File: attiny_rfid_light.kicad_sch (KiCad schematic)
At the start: 26 parts, among them IC1 EM4095, U1 ESP32-WROOM-32, U2 NCP1117-3.3_SOT223

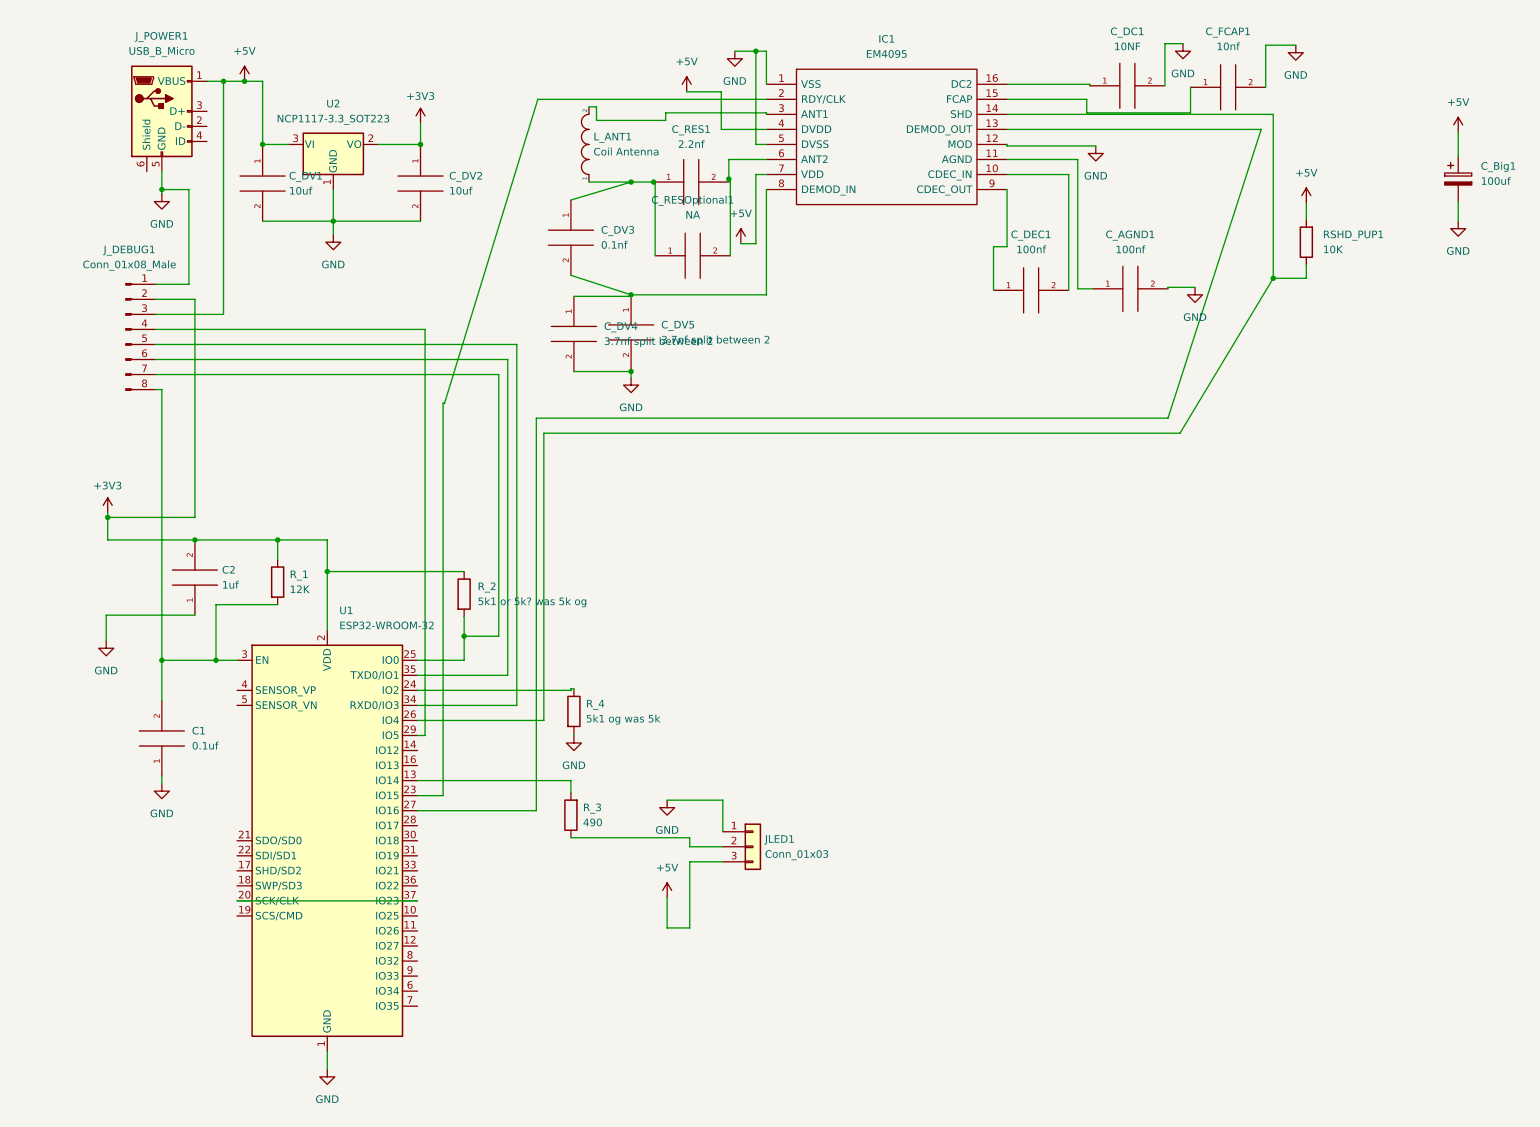
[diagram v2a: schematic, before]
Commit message: updated values to match place values
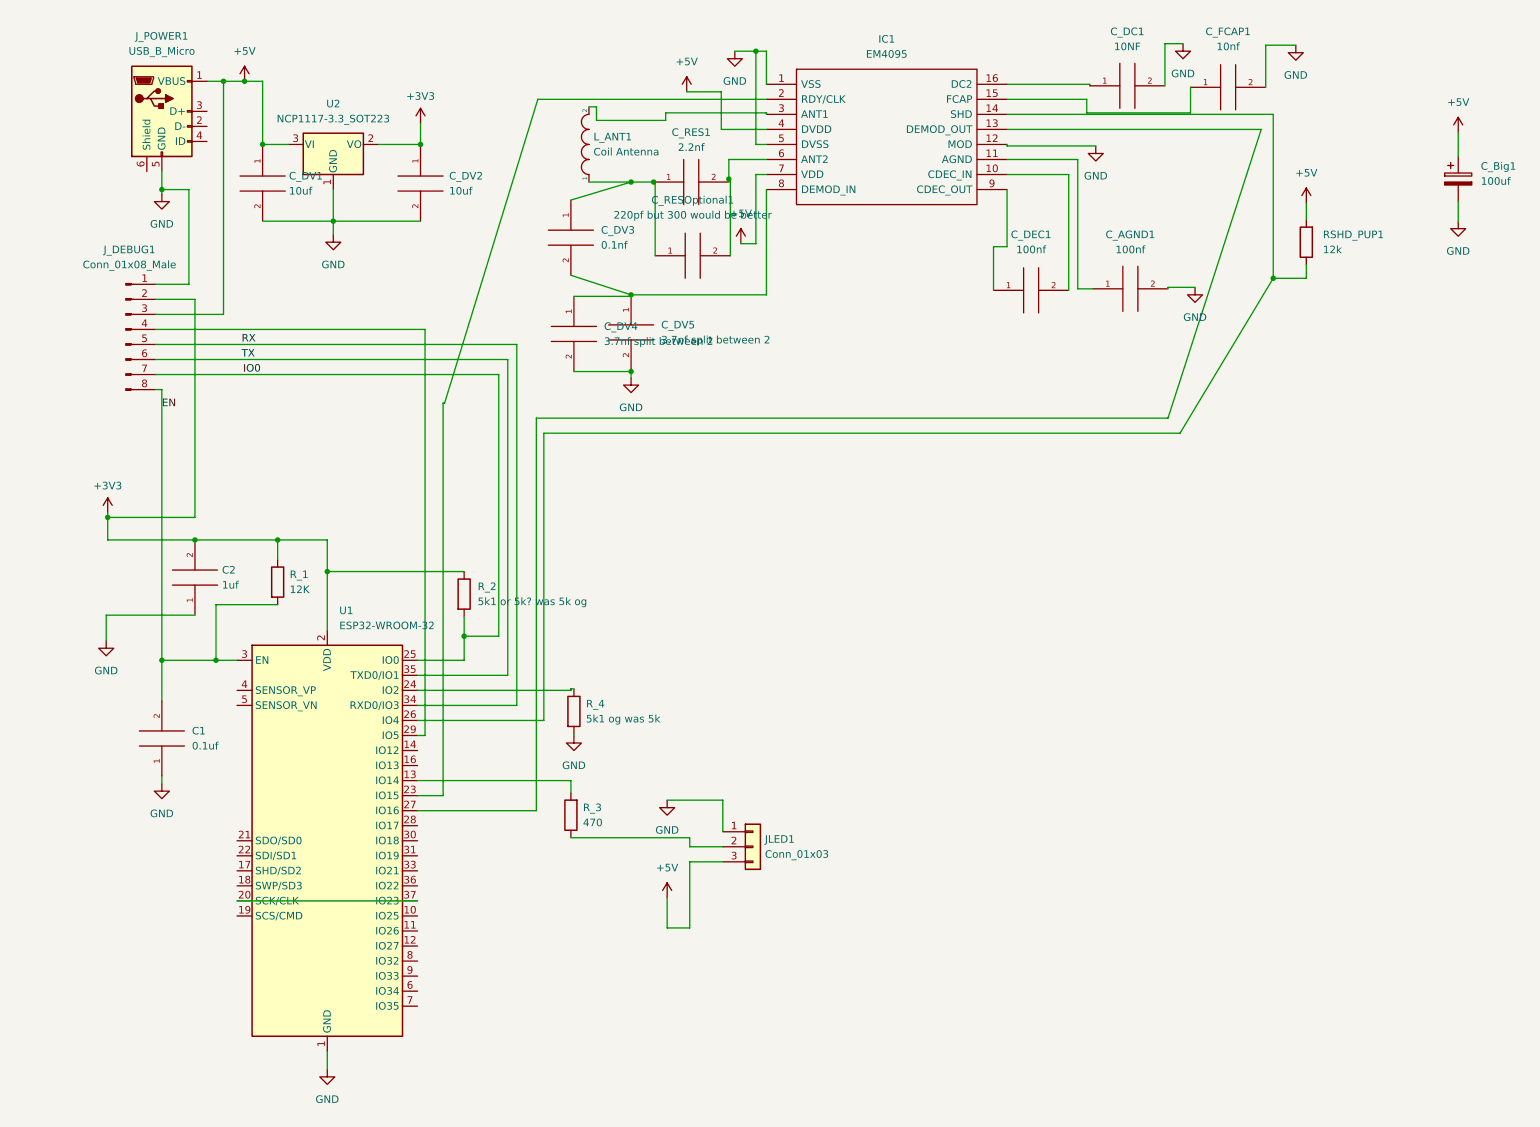
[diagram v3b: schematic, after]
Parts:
- C_RESOptional1: value NA -> 220pf but 300 would be better
- RSHD_PUP1: value 10K -> 12k
- R_3: value 490 -> 470
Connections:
- net RX: now reaches J_DEBUG1.5 (Pin_5), U1.34 (RXD0/IO3)
- net TX: now reaches J_DEBUG1.6 (Pin_6), U1.35 (TXD0/IO1)
- net IO0: now reaches J_DEBUG1.7 (Pin_7), R_2.2, U1.25 (IO0)
- net EN: now reaches C1.2, J_DEBUG1.8 (Pin_8), R_1.2, U1.3 (EN)
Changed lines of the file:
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@@
     (stroke (width 0) (type default) (color 0 0 0 0))
+  )
+  (label "TX" (at 43.942 70.104 0)
+    (effects (font (size 1.27 1.27)) (justify left bottom))
+  )
+  (label "IO0" (at 44.196 72.644 0)
+    (effects (font (size 1.27 1.27)) (justify left bottom))
+  )
+  (label "RX" (at 43.942 67.564 0)
+    (effects (font (size 1.27 1.27)) (justify left bottom))
+  )
+  (label "EN" (at 30.48 78.486 0)
+    (effects (font (size 1.27 1.27)) (justify left bottom))
   )
   (symbol (lib_id "Connector:Conn_01x08_Male") (at 24.384 65.024 0) (unit 1)
@@
       (effects (font (size 1.27 1.27)) (justify right))
     )
-    (property "Value" "10K" (id 1) (at 226.568 51.5619 0)
+    (property "Value" "12k" (id 1) (at 226.568 51.5619 0)
       (effects (font (size 1.27 1.27)) (justify right))
     )
@@
     (in_bom yes) (on_board yes) (fields_autoplaced)
     (property "Reference" "C_RESOptional1" (id 0) (at 120.142 43.18 90))
-    (property "Value" "NA" (id 1) (at 120.142 45.72 90))
+    (property "Value" "220pf but 300 would be better" (id 1) (at 120.142 45.72 90))
     (property "Footprint" "Capacitor_SMD:C_0805_2012Metric_Pad1.18x1.45mm_HandSolder" (id 2) (at 120.142 52.578 0)
       (effects (font (size 1.27 1.27)) hide)
@@
       (effects (font (size 1.27 1.27)) (justify right))
     )
-    (property "Value" "490" (id 1) (at 101.6 148.3359 0)
+    (property "Value" "470" (id 1) (at 101.6 148.3359 0)
       (effects (font (size 1.27 1.27)) (justify right))
     )
@@
   (symbol (lib_id "pspice:C") (at 119.888 40.132 90) (unit 1)
     (in_bom yes) (on_board yes) (fields_autoplaced)
-    (property "Reference" "C_RES1" (id 0) (at 119.888 31.242 90))
-    (property "Value" "2.2nf" (id 1) (at 119.888 33.782 90))
+    (property "Reference" "C_RES1" (id 0) (at 119.888 31.75 90))
+    (property "Value" "2.2nf" (id 1) (at 119.888 34.29 90))
     (property "Footprint" "Capacitor_SMD:C_0805_2012Metric_Pad1.18x1.45mm_HandSolder" (id 2) (at 119.888 40.132 0)
       (effects (font (size 1.27 1.27)) hide)
@@
     )
     (path "/9f822722-8d50-42f5-a09c-1e6f990511b7"
-      (reference "C_RESOptional1") (unit 1) (value "NA") (footprint "Capacitor_SMD:C_0805_2012Metric_Pad1.18x1.45mm_HandSolder")
+      (reference "C_RESOptional1") (unit 1) (value "220pf but 300 would be better") (footprint "Capacitor_SMD:C_0805_2012Metric_Pad1.18x1.45mm_HandSolder")
     )
     (path "/72ff0485-f700-4243-a66c-13414af86c8f"
@@
     )
     (path "/81c65984-9f9d-492c-82f9-bbe24b88ebc2"
-      (reference "RSHD_PUP1") (unit 1) (value "10K") (footprint "Resistor_SMD:R_0805_2012Metric_Pad1.20x1.40mm_HandSolder")
+      (reference "RSHD_PUP1") (unit 1) (value "12k") (footprint "Resistor_SMD:R_0805_2012Metric_Pad1.20x1.40mm_HandSolder")
     )
     (path "/b2b8605e-6475-43cb-8fde-09cbdf493df9"
@@
     )
     (path "/ae4d83e7-2b1c-4a1b-a2e3-a202e2758c5c"
-      (reference "R_3") (unit 1) (value "490") (footprint "Resistor_SMD:R_0805_2012Metric_Pad1.20x1.40mm_HandSolder")
+      (reference "R_3") (unit 1) (value "470") (footprint "Resistor_SMD:R_0805_2012Metric_Pad1.20x1.40mm_HandSolder")
     )
     (path "/6eacda91-754b-4c18-b3d0-a8600716fb2d"

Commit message: v4
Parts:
- removed J_DEBUG1: Conn_01x08_Male, Connector_PinHeader_2.54mm:PinHeader_1x08_P2.54mm_Vertical, symbol Connector:Conn_01x08_Male
- added C_RESC1: optional, Capacitor_SMD:C_0805_2012Metric_Pad1.18x1.45mm_HandSolder, symbol pspice:C
- added J1: Conn_01x16_Male, Connector_PinHeader_2.54mm:PinHeader_1x16_P2.54mm_Vertical, symbol Connector:Conn_01x16_Male
- added RMOD1: 10k, Resistor_SMD:R_0805_2012Metric_Pad1.20x1.40mm_HandSolder, symbol Device:R
- C_Big1: footprint Capacitor_THT:C_Radial_D5.0mm_H11.0mm_P2.00mm -> Capacitor_SMD:CP_Elec_8x10.5
- C_RESB1: renamed from C_RESOptional1; value 220pf but 300 would be better -> 300pf
- J_POWER1: footprint Connector_USB:USB_Micro-B_Molex-105017-0001 -> Connector_USB:USB_Micro-B_Molex_47346-0001
- R_2: value 5k1 or 5k? was 5k og -> 5k1
- R_4: value 5k1 og was 5k -> 5k1
- renumbered C_DV1 to C_REG1, C_DV2 to C_REG2, C_RES1 to C_RESA1
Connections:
- net +3V3: now also J1.2 (Pin_2)
- net +5V: now also J1.3 (Pin_3)
- net EN: now also J1.8 (Pin_8)
- net GND: now also J1.1 (Pin_1), RMOD1.1; no longer IC1.12 (MOD)
- net IO0: now also J1.7 (Pin_7)
- net RX: now also J1.5 (Pin_5)
- net TX: now also J1.6 (Pin_6)
- net 5: now reaches U1.29 (IO5)
- net 5: now also J1.4 (Pin_4)
- net DEMOD_OUT: now reaches IC1.13 (DEMOD_OUT), U1.27 (IO16)
- net SHD: now reaches IC1.14 (SHD), RSHD_PUP1.1, U1.26 (IO4)
- net RDY_CLK: now reaches IC1.2 (RDY/CLK), U1.23 (IO15)
- net at C_RESA1.2, C_RESB1.2, IC1.6 (ANT2): now also C_RESC1.1
- net at C_DV3.1, C_RESA1.1, C_RESB1.1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: now also C_RESC1.2
- net 25: now reaches U1.10 (IO25)
- net 25: now also J1.13 (Pin_13)
- net 26: now reaches U1.11 (IO26)
- net 26: now also J1.14 (Pin_14)
- net MOD: now reaches U1.12 (IO27)
- net MOD: now also IC1.12 (MOD), RMOD1.2
- net 18: now reaches U1.30 (IO18)
- net 18: now also J1.12 (Pin_12)
- net 19: now reaches U1.31 (IO19)
- net 19: now also J1.11 (Pin_11)
- net 21: now reaches U1.33 (IO21)
- net 21: now also J1.10 (Pin_10)
- net 22: now reaches U1.36 (IO22)
- net 22: now also J1.9 (Pin_9)
- net 32: now reaches U1.8 (IO32)
- net 32: now also J1.16 (Pin_16)
- net 33: now reaches U1.9 (IO33)
- net 33: now also J1.15 (Pin_15)

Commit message: v5
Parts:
- C_DV4: value 3.7nf split between 2 -> 3.6nf
- C_DV5: value 3.7nf split between 2 -> optional
- C_RESB1: value 300pf -> 470pf
- RMOD1: value 10k -> 12k
- U1: value ESP32-WROOM-32 -> ESP32S3-WROOM-32
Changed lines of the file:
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@@
   (symbol (lib_id "pspice:C") (at 109.728 65.532 0) (unit 1)
     (in_bom yes) (on_board yes) (fields_autoplaced)
-    (property "Reference" "C_DV5" (id 0) (at 114.808 64.2619 0)
-      (effects (font (size 1.27 1.27)) (justify left))
-    )
-    (property "Value" "3.7nf split between 2" (id 1) (at 114.808 66.8019 0)
+    (property "Reference" "C_DV5" (id 0) (at 114.3 64.2619 0)
+      (effects (font (size 1.27 1.27)) (justify left))
+    )
+    (property "Value" "optional" (id 1) (at 114.3 66.8019 0)
       (effects (font (size 1.27 1.27)) (justify left))
     )
@@
   (symbol (lib_id "power:GND") (at 197.358 41.656 0) (unit 1)
     (in_bom yes) (on_board yes) (fields_autoplaced)
-    (property "Reference" "#PWR?" (id 0) (at 197.358 48.006 0)
+    (property "Reference" "#PWR0101" (id 0) (at 197.358 48.006 0)
       (effects (font (size 1.27 1.27)) hide)
     )
@@
   (symbol (lib_id "Device:R") (at 223.774 50.292 180) (unit 1)
     (in_bom yes) (on_board yes) (fields_autoplaced)
-    (property "Reference" "RSHD_PUP1" (id 0) (at 226.568 49.0219 0)
-      (effects (font (size 1.27 1.27)) (justify right))
-    )
-    (property "Value" "12k" (id 1) (at 226.568 51.5619 0)
+    (property "Reference" "RSHD_PUP1" (id 0) (at 226.06 49.0219 0)
+      (effects (font (size 1.27 1.27)) (justify right))
+    )
+    (property "Value" "12k" (id 1) (at 226.06 51.5619 0)
       (effects (font (size 1.27 1.27)) (justify right))
     )
@@
     (in_bom yes) (on_board yes) (fields_autoplaced)
     (property "Reference" "C_RESB1" (id 0) (at 120.142 43.18 90))
-    (property "Value" "300pf" (id 1) (at 120.142 45.72 90))
+    (property "Value" "470pf" (id 1) (at 120.142 45.72 90))
     (property "Footprint" "Capacitor_SMD:C_0805_2012Metric_Pad1.18x1.45mm_HandSolder" (id 2) (at 120.142 52.578 0)
       (effects (font (size 1.27 1.27)) hide)
@@
       (effects (font (size 1.27 1.27)) (justify right))
     )
-    (property "Value" "10k" (id 1) (at 199.39 39.1159 0)
+    (property "Value" "12k" (id 1) (at 199.39 39.1159 0)
       (effects (font (size 1.27 1.27)) (justify right))
     )
@@
       (effects (font (size 1.27 1.27)) (justify left))
     )
-    (property "Value" "ESP32-WROOM-32" (id 1) (at 60.4394 115.062 0)
+    (property "Value" "ESP32S3-WROOM-32" (id 1) (at 60.4394 115.062 0)
       (effects (font (size 1.27 1.27)) (justify left))
     )
@@
   (symbol (lib_id "pspice:C") (at 100.076 65.786 0) (unit 1)
     (in_bom yes) (on_board yes) (fields_autoplaced)
-    (property "Reference" "C_DV4" (id 0) (at 105.156 64.5159 0)
-      (effects (font (size 1.27 1.27)) (justify left))
-    )
-    (property "Value" "3.7nf split between 2" (id 1) (at 105.156 67.0559 0)
+    (property "Reference" "C_DV4" (id 0) (at 105.41 64.5159 0)
+      (effects (font (size 1.27 1.27)) (justify left))
+    )
+    (property "Value" "3.6nf" (id 1) (at 105.41 67.0559 0)
       (effects (font (size 1.27 1.27)) (justify left))
     )
@@
     )
     (path "/22d7c125-9cf1-4deb-b5d5-b51921c98da9"
-      (reference "#PWR?") (unit 1) (value "GND") (footprint "")
+      (reference "#PWR0101") (unit 1) (value "GND") (footprint "")
     )
     (path "/64dd7740-0c72-400b-88d0-286b4c64ef49"
@@
     )
     (path "/fd781061-b786-4aa7-81c8-507570ec21b2"
-      (reference "C_DV4") (unit 1) (value "3.7nf split between 2") (footprint "Capacitor_SMD:C_0805_2012Metric_Pad1.18x1.45mm_HandSolder")
+      (reference "C_DV4") (unit 1) (value "3.6nf") (footprint "Capacitor_SMD:C_0805_2012Metric_Pad1.18x1.45mm_HandSolder")
     )
     (path "/0970727f-11dd-473f-b585-f40294eee11b"
-      (reference "C_DV5") (unit 1) (value "3.7nf split between 2") (footprint "Capacitor_SMD:C_0805_2012Metric_Pad1.18x1.45mm_HandSolder")
+      (reference "C_DV5") (unit 1) (value "optional") (footprint "Capacitor_SMD:C_0805_2012Metric_Pad1.18x1.45mm_HandSolder")
     )
     (path "/5fade6ac-277b-43df-8e3a-ea7ae9efe0a9"
@@
     )
     (path "/9f822722-8d50-42f5-a09c-1e6f990511b7"
-      (reference "C_RESB1") (unit 1) (value "300pf") (footprint "Capacitor_SMD:C_0805_2012Metric_Pad1.18x1.45mm_HandSolder")
+      (reference "C_RESB1") (unit 1) (value "470pf") (footprint "Capacitor_SMD:C_0805_2012Metric_Pad1.18x1.45mm_HandSolder")
     )
     (path "/a97e32ce-d185-4613-bc22-b319deb2b8c6"
@@
     )
     (path "/b5d9e330-bd91-4c98-8aec-669ce9e63550"
-      (reference "RMOD1") (unit 1) (value "10k") (footprint "Resistor_SMD:R_0805_2012Metric_Pad1.20x1.40mm_HandSolder")
+      (reference "RMOD1") (unit 1) (value "12k") (footprint "Resistor_SMD:R_0805_2012Metric_Pad1.20x1.40mm_HandSolder")
     )
     (path "/81c65984-9f9d-492c-82f9-bbe24b88ebc2"
@@
     )
     (path "/dd8613f5-26c5-442c-934d-db0fe188f421"
-      (reference "U1") (unit 1) (value "ESP32-WROOM-32") (footprint "RF_Module:ESP32-WROOM-32")
+      (reference "U1") (unit 1) (value "ESP32S3-WROOM-32") (footprint "RF_Module:ESP32-WROOM-32")
     )
     (path "/d2fc0903-7aa6-406c-9d43-15f34b985517"
